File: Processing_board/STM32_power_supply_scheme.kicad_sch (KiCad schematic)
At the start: 15 parts

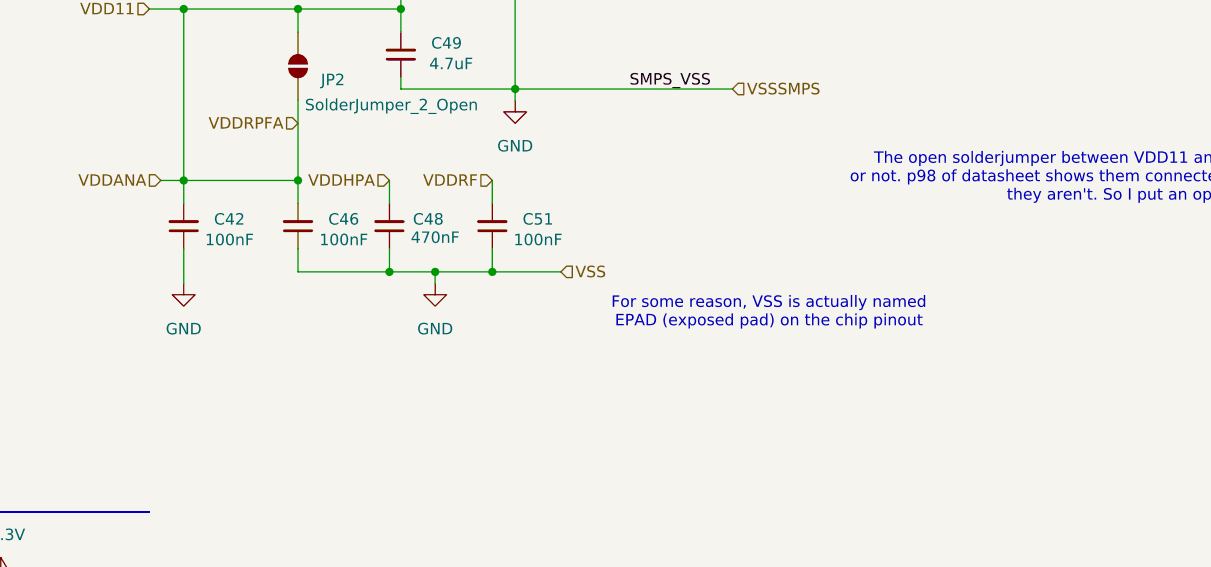
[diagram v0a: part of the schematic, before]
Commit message: connected VDDRF to 3V3, but errors still remaining
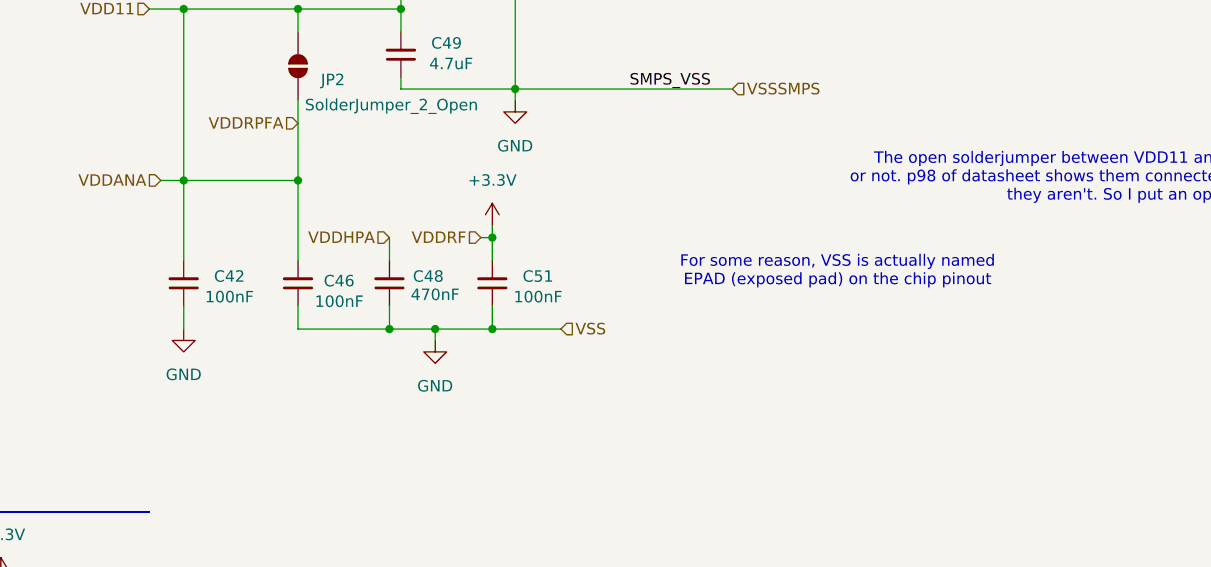
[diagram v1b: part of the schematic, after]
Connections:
- net VDDRF is gone; now on net +3.3V: C51.2
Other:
- moved on the sheet: C42, C46, C48, C51

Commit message: feat: finalized ADC design
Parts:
- C40, C41, C42, C43, C44, C45, C46, C47, C48, C49, C50, C51, C52: footprint Capacitor_SMD:C_0402_1005Metric -> Capacitor_SMD:C_0201_0603Metric_Pad0.64x0.40mm_HandSolder
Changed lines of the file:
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@@
 			)
 		)
-		(property "Footprint" "Capacitor_SMD:C_0402_1005Metric"
+		(property "Footprint" "Capacitor_SMD:C_0201_0603Metric_Pad0.64x0.40mm_HandSolder"
 			(at 138.43 107.95 0)
 			(effects
@@
 			)
 		)
-		(property "Footprint" "Capacitor_SMD:C_0402_1005Metric"
+		(property "Footprint" "Capacitor_SMD:C_0201_0603Metric_Pad0.64x0.40mm_HandSolder"
 			(at 111.76 147.32 0)
 			(effects
@@
 			)
 		)
-		(property "Footprint" "Capacitor_SMD:C_0402_1005Metric"
+		(property "Footprint" "Capacitor_SMD:C_0201_0603Metric_Pad0.64x0.40mm_HandSolder"
 			(at 123.19 39.37 0)
 			(effects
@@
 			)
 		)
-		(property "Footprint" "Capacitor_SMD:C_0402_1005Metric"
+		(property "Footprint" "Capacitor_SMD:C_0201_0603Metric_Pad0.64x0.40mm_HandSolder"
 			(at 114.3 39.37 0)
 			(effects
@@
 			)
 		)
-		(property "Footprint" "Capacitor_SMD:C_0402_1005Metric"
+		(property "Footprint" "Capacitor_SMD:C_0201_0603Metric_Pad0.64x0.40mm_HandSolder"
 			(at 128.27 82.55 0)
 			(effects
@@
 			)
 		)
-		(property "Footprint" "Capacitor_SMD:C_0402_1005Metric"
+		(property "Footprint" "Capacitor_SMD:C_0201_0603Metric_Pad0.64x0.40mm_HandSolder"
 			(at 104.14 107.95 0)
 			(effects
@@
 			)
 		)
-		(property "Footprint" "Capacitor_SMD:C_0402_1005Metric"
+		(property "Footprint" "Capacitor_SMD:C_0201_0603Metric_Pad0.64x0.40mm_HandSolder"
 			(at 97.79 39.37 0)
 			(effects
@@
 			)
 		)
-		(property "Footprint" "Capacitor_SMD:C_0402_1005Metric"
+		(property "Footprint" "Capacitor_SMD:C_0201_0603Metric_Pad0.64x0.40mm_HandSolder"
 			(at 133.35 39.37 0)
 			(effects
@@
 			)
 		)
-		(property "Footprint" "Capacitor_SMD:C_0402_1005Metric"
+		(property "Footprint" "Capacitor_SMD:C_0201_0603Metric_Pad0.64x0.40mm_HandSolder"
 			(at 127 107.95 0)
 			(effects
@@
 			)
 		)
-		(property "Footprint" "Capacitor_SMD:C_0402_1005Metric"
+		(property "Footprint" "Capacitor_SMD:C_0201_0603Metric_Pad0.64x0.40mm_HandSolder"
 			(at 101.6 147.32 0)
 			(effects
@@
 			)
 		)
-		(property "Footprint" "Capacitor_SMD:C_0402_1005Metric"
+		(property "Footprint" "Capacitor_SMD:C_0201_0603Metric_Pad0.64x0.40mm_HandSolder"
 			(at 140.97 69.85 0)
 			(effects
@@
 			)
 		)
-		(property "Footprint" "Capacitor_SMD:C_0402_1005Metric"
+		(property "Footprint" "Capacitor_SMD:C_0201_0603Metric_Pad0.64x0.40mm_HandSolder"
 			(at 116.84 107.95 0)
 			(effects
@@
 			)
 		)
-		(property "Footprint" "Capacitor_SMD:C_0402_1005Metric"
+		(property "Footprint" "Capacitor_SMD:C_0201_0603Metric_Pad0.64x0.40mm_HandSolder"
 			(at 105.41 39.37 0)
 			(effects
